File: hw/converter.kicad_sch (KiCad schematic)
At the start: 13 parts, among them J301 1935776, J302 1935776, Q301 SW_L, Q302 SW_H

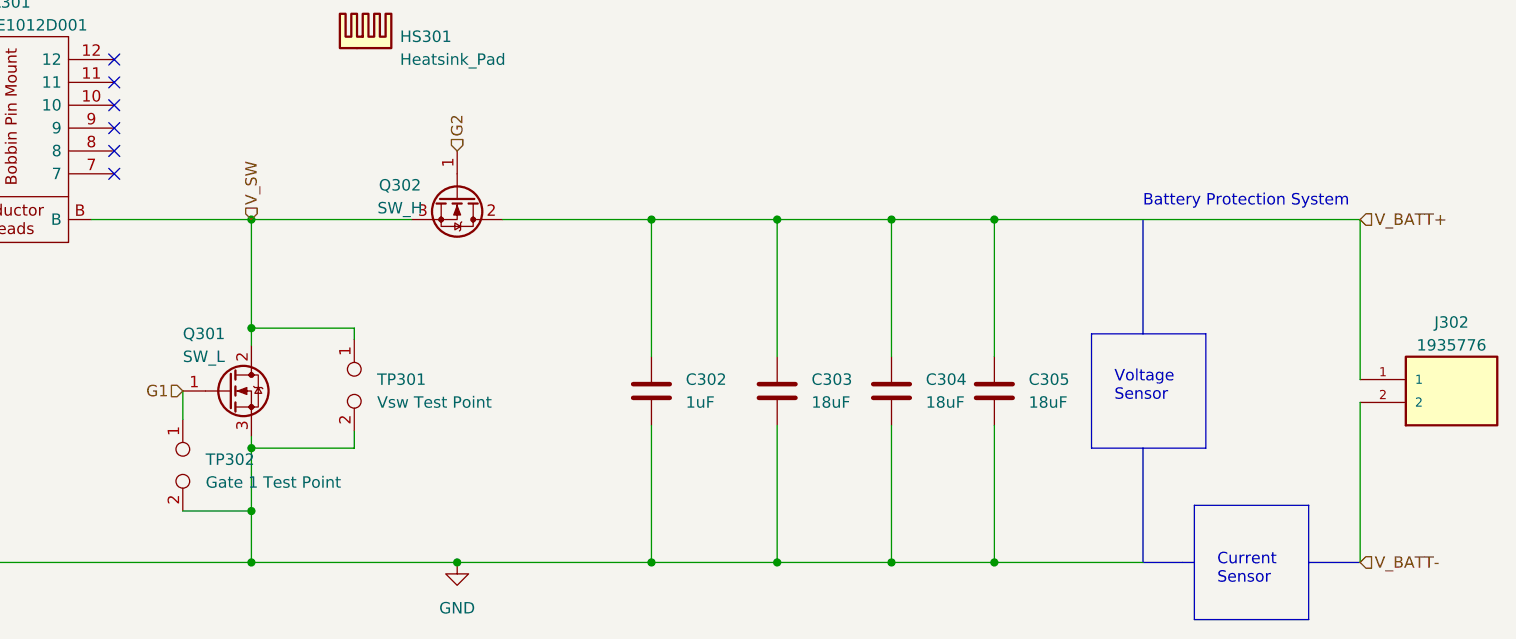
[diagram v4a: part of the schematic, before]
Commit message: rebuild schematic, passes ERC, bom completed
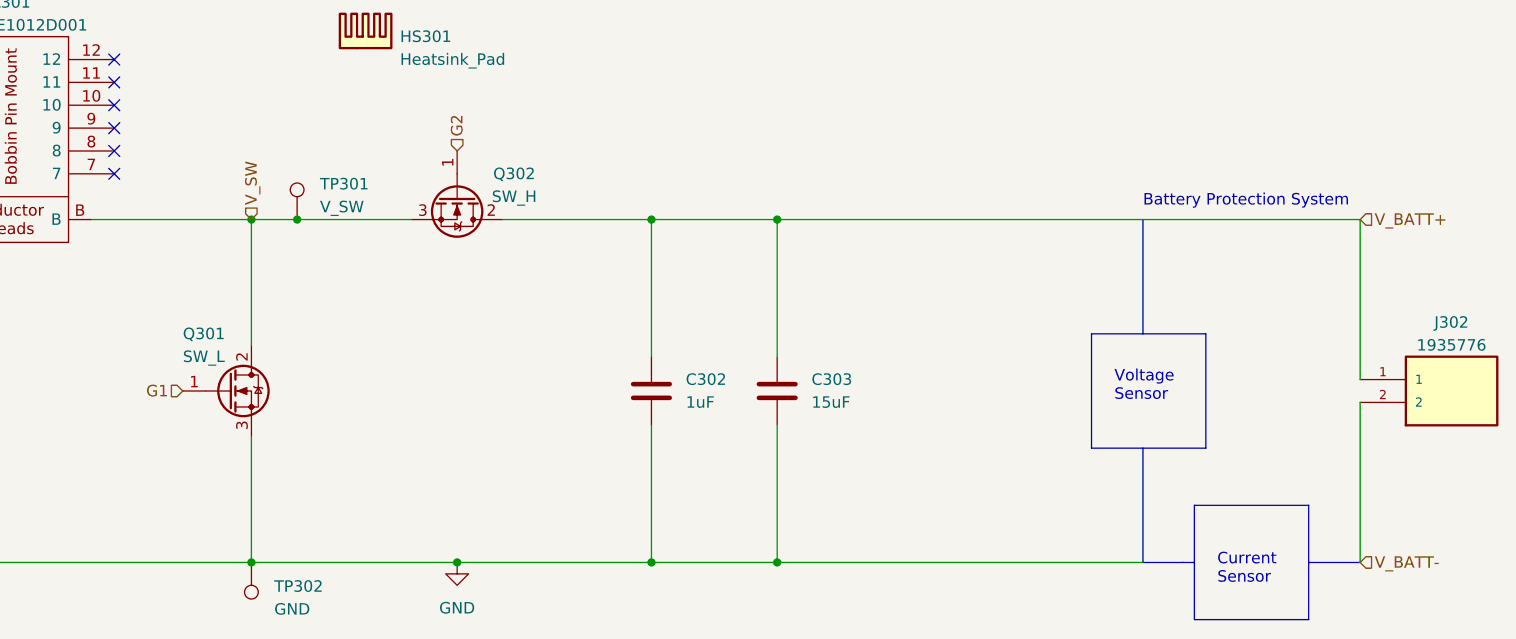
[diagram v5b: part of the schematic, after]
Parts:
- removed C304, C305: 18uF, Capacitor_THT:CP_Radial_D10.0mm_P5.00mm, symbol Device:C
- removed TP301: Vsw Test Point, mppt:SignalTP, symbol Connector:TestPoint_2Pole
- removed TP302: Gate 1 Test Point, mppt:SignalTP, symbol Connector:TestPoint_2Pole
- added TP301: V_SW, TestPoint:TestPoint_Keystone_5000-5004_Miniature, symbol Connector:TestPoint
- added TP302: GND, TestPoint:TestPoint_Keystone_5000-5004_Miniature, symbol Connector:TestPoint
- C301: footprint Capacitor_THT:CP_Axial_L10.0mm_D6.0mm_P15.00mm_Horizontal -> Capacitor_THT:C_Rect_L11.5mm_W5.6mm_P10.00mm_MKT; Distributor (none) -> Mouser; Manufacturer (none) -> Cornell Dubilier; P/N (none) -> 598-RA4505K100-FA
- C302: Distributor (none) -> Mouser; Manufacturer (none) -> TDK; P/N (none) -> 810-CGA9P3X7T2E225MA
- C303: value 18uF -> 15uF; footprint Capacitor_THT:CP_Radial_D10.0mm_P5.00mm -> Capacitor_THT:C_Rect_L41.5mm_W20.0mm_P37.50mm_MKS4; Distributor (none) -> Mouser; Manufacturer (none) -> KEMET; P/N (none) -> 80-R75GW515050H0J
- HS301: Distributor (none) -> Amazon; Manufacturer (none) -> WayInTop; P/N (none) -> N/A
- J301, J302: footprint 1935776 -> mppt:1935776; DESCRIPTION Fixed Terminal Blocks PT 2.5/ 2-5.0-H g -> (none); Distributor (none) -> Mouser; HEIGHT 13.5mm -> (none); MANUFACTURER_NAME Phoenix Contact -> (none); MANUFACTURER_PART_NUMBER 1935776 -> (none); MOUSER_PART_NUMBER 651-1935776 -> (none); MOUSER_PRICE-STOCK https://www.mouser.co.uk/ProductDetail/Phoenix-Contact/1935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 -> (none); Manufacturer (none) -> Phoenix Contact; P/N (none) -> 651-1935776
- L301: Distributor (none) -> Mouser; Height 29.3 -> (none); Manufacturer (none) -> EPCOS/TDK; Manufacturer_Name TDK -> (none); Manufacturer_Part_Number B65878E1012D001 -> (none); Mouser Part Number 871-B65878E1012D001 -> (none); Mouser Price/Stock https://www.mouser.co.uk/ProductDetail/EPCOS-TDK/B65878E101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 -> (none); P/N (none) -> 871-B65877A0000R097 / 871-B65878E1012D001
- Q301, Q302: Distributor (none) -> Digikey; Manufacturer (none) -> EPC; P/N (none) -> 917-EPC2307ENGRTTR-ND
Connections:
- net GND: now also TP302.1
- net V_SW: now also TP301.1

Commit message: savestate layout
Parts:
- removed TP301: V_SW, TestPoint:TestPoint_Keystone_5000-5004_Miniature, symbol Connector:TestPoint
- removed TP302: GND, TestPoint:TestPoint_Keystone_5000-5004_Miniature, symbol Connector:TestPoint
- added TP301: TestPoint_2Pole, mppt:SignalTP, symbol Connector:TestPoint_2Pole
- C303: value 15uF -> 18uF; footprint Capacitor_THT:C_Rect_L41.5mm_W20.0mm_P37.50mm_MKS4 -> Capacitor_THT:C_Radial_D10.0mm_H16.0mm_P5.00mm; P/N 80-R75GW515050H0J -> 80-A759MS186M2CAAE90
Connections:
- net GND: now also TP301.2
- net V_SW: now also TP301.1
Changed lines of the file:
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@@
   (junction (at 191.77 109.22) (diameter 0) (color 0 0 0 0)
   )
-  (junction (at 138.43 71.12) (diameter 0) (color 0 0 0 0)
-  )
   (junction (at 80.01 109.22) (diameter 0) (color 0 0 0 0)
   )
@@
   (junction (at 133.35 71.12) (diameter 0) (color 0 0 0 0)
   )
+  (junction (at 133.35 85.09) (diameter 0) (color 0 0 0 0)
+  )
   (junction (at 133.35 109.22) (diameter 0) (color 0 0 0 0)
   )
@@
   )
   (junction (at 156.21 109.22) (diameter 0) (color 0 0 0 0)
+  )
+  (junction (at 133.35 95.25) (diameter 0) (color 0 0 0 0)
   )
   (junction (at 177.8 109.22) (diameter 0) (color 0 0 0 0)
@@
     (stroke (width 0) (type default))
   )
+  (wire (pts (xy 133.35 85.09) (xy 140.97 85.09))
+    (stroke (width 0) (type default))
+  )
   (wire (pts (xy 40.64 91.44) (xy 40.64 109.22))
     (stroke (width 0) (type default))
@@
     (stroke (width 0) (type default))
   )
-  (wire (pts (xy 133.35 71.12) (xy 138.43 71.12))
+  (wire (pts (xy 133.35 71.12) (xy 151.13 71.12))
     (stroke (width 0) (type default))
   )
@@
     (stroke (width 0) (type default))
   )
-  (wire (pts (xy 138.43 71.12) (xy 151.13 71.12))
-    (stroke (width 0) (type default))
-  )
   (wire (pts (xy 80.01 109.22) (xy 80.01 93.98))
     (stroke (width 0) (type default))
@@
   )
   (polyline (pts (xy 60.325 115.57) (xy 47.625 115.57))
+    (stroke (width 0) (type default))
+  )
+  (wire (pts (xy 133.35 95.25) (xy 140.97 95.25))
     (stroke (width 0) (type default))
   )
@@
     )
   )
-  (symbol (lib_id "Connector:TestPoint") (at 133.35 109.22 180) (unit 1)
-    (in_bom yes) (on_board yes) (dnp no) (fields_autoplaced)
-    (property "Reference" "TP302" (at 135.89 111.887 0)
-      (effects (font (size 1.27 1.27)) (justify right))
-    )
-    (property "Value" "GND" (at 135.89 114.427 0)
-      (effects (font (size 1.27 1.27)) (justify right))
-    )
-    (property "Footprint" "TestPoint:TestPoint_Keystone_5000-5004_Miniature" (at 128.27 109.22 0)
-      (effects (font (size 1.27 1.27)) hide)
-    )
-    (property "Datasheet" "https://www.mouser.com/datasheet/2/215/000-5004-741181.pdf" (at 128.27 109.22 0)
-      (effects (font (size 1.27 1.27)) hide)
-    )
-    (property "Color" "Black" (at 133.35 109.22 0)
-      (effects (font (size 1.27 1.27)) hide)
-    )
-    (property "Distributor" "Mouser" (at 133.35 109.22 0)
-      (effects (font (size 1.27 1.27)) hide)
-    )
-    (property "Manufacturer" "Keystone Electronics" (at 133.35 109.22 0)
-      (effects (font (size 1.27 1.27)) hide)
-    )
-    (property "P/N" "534-5001" (at 133.35 109.22 0)
-      (effects (font (size 1.27 1.27)) hide)
-    )
-    (pin "1")
-    (instances
-      (project "mppt"
-        (path "/06fd3a42-664d-41bc-bf0f-b5ee0ddcc902/9cd55a57-0ec8-481d-b571-b5fdbe353ce7"
-          (reference "TP302") (unit 1)
-        )
-      )
-    )
-  )
   (symbol (lib_id "Device:C") (at 177.8 90.17 0) (unit 1)
     (in_bom yes) (on_board yes) (dnp no)
@@
     )
   )
-  (symbol (lib_id "Connector:TestPoint") (at 138.43 71.12 0) (unit 1)
-    (in_bom yes) (on_board yes) (dnp no) (fields_autoplaced)
-    (property "Reference" "TP301" (at 140.97 67.183 0)
-      (effects (font (size 1.27 1.27)) (justify left))
-    )
-    (property "Value" "V_SW" (at 140.97 69.723 0)
-      (effects (font (size 1.27 1.27)) (justify left))
-    )
-    (property "Footprint" "TestPoint:TestPoint_Keystone_5000-5004_Miniature" (at 143.51 71.12 0)
-      (effects (font (size 1.27 1.27)) hide)
-    )
-    (property "Datasheet" "https://www.mouser.com/datasheet/2/215/5115_5119-741190.pdf" (at 143.51 71.12 0)
-      (effects (font (size 1.27 1.27)) hide)
-    )
-    (property "Color" "Purple" (at 138.43 71.12 0)
-      (effects (font (size 1.27 1.27)) hide)
-    )
-    (property "Distributor" "Mouser" (at 138.43 71.12 0)
-      (effects (font (size 1.27 1.27)) hide)
-    )
-    (property "Manufacturer" "Keystone Electronics" (at 138.43 71.12 0)
-      (effects (font (size 1.27 1.27)) hide)
-    )
-    (property "P/N" "534-5119" (at 138.43 71.12 0)
-      (effects (font (size 1.27 1.27)) hide)
-    )
-    (pin "1")
-    (instances
-      (project "mppt"
-        (path "/06fd3a42-664d-41bc-bf0f-b5ee0ddcc902/9cd55a57-0ec8-481d-b571-b5fdbe353ce7"
-          (reference "TP301") (unit 1)
-        )
-      )
-    )
-  )
   (symbol (lib_id "Device:Q_NMOS_GDS") (at 156.21 68.58 270) (unit 1)
     (in_bom yes) (on_board yes) (dnp no)
@@
     )
   )
+  (symbol (lib_id "Connector:TestPoint_2Pole") (at 140.97 90.17 270) (unit 1)
+    (in_bom yes) (on_board yes) (dnp no) (fields_autoplaced)
+    (property "Reference" "TP301" (at 143.51 89.535 90)
+      (effects (font (size 1.27 1.27)) (justify left))
+    )
+    (property "Value" "TestPoint_2Pole" (at 143.51 92.075 90)
+      (effects (font (size 1.27 1.27)) (justify left))
+    )
+    (property "Footprint" "mppt:SignalTP" (at 140.97 90.17 0)
+      (effects (font (size 1.27 1.27)) hide)
+    )
+    (property "Datasheet" "~" (at 140.97 90.17 0)
+      (effects (font (size 1.27 1.27)) hide)
+    )
+    (pin "1")
+    (pin "2")
+    (instances
+      (project "mppt"
+        (path "/06fd3a42-664d-41bc-bf0f-b5ee0ddcc902/9cd55a57-0ec8-481d-b571-b5fdbe353ce7"
+          (reference "TP301") (unit 1)
+        )
+      )
+    )
+  )
   (symbol (lib_id "Device:C") (at 80.01 90.17 0) (unit 1)
     (in_bom yes) (on_board yes) (dnp no) (fields_autoplaced)
@@
       (effects (font (size 1.27 1.27)) (justify left))
     )
-    (property "Value" "15uF" (at 195.58 91.4399 0)
-      (effects (font (size 1.27 1.27)) (justify left))
-    )
-    (property "Footprint" "Capacitor_THT:C_Rect_L41.5mm_W20.0mm_P37.50mm_MKS4" (at 192.7352 93.98 0)
-      (effects (font (size 1.27 1.27)) hide)
-    )
-    (property "Datasheet" "https://www.mouser.com/datasheet/2/212/1/KEM_F3121_R75H-1879088.pdf" (at 191.77 90.17 0)
+    (property "Value" "18uF" (at 195.58 91.4399 0)
+      (effects (font (size 1.27 1.27)) (justify left))
+    )
+    (property "Footprint" "Capacitor_THT:C_Radial_D10.0mm_H16.0mm_P5.00mm" (at 192.7352 93.98 0)
+      (effects (font (size 1.27 1.27)) hide)
+    )
+    (property "Datasheet" "https://www.mouser.com/datasheet/2/212/KEM_A4072_A759-1104329.pdf" (at 191.77 90.17 0)
       (effects (font (size 1.27 1.27)) hide)
     )
@@
       (effects (font (size 1.27 1.27)) hide)
     )
-    (property "P/N" "80-R75GW515050H0J" (at 191.77 90.17 0)
-      (effects (font (size 1.27 1.27)) hide)
-    )
+    (property "P/N" "80-A759MS186M2CAAE90" (at 191.77 90.17 0)
+      (effects (font (size 1.27 1.27)) hide)
+    )

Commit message: final layout
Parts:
- added C302: CP, Capacitor_THT:C_Radial_D10.0mm_H12.5mm_P5.00mm, symbol Device:C
- added D301: Schottky, Diode_THT:D_5W_P5.08mm_Vertical_AnodeUp, symbol Device:D_Schottky
- added R301: R, Resistor_THT:R_Radial_Power_L11.0mm_W7.0mm_P5.00mm, symbol Device:R
- added TP410: TestPoint_2Pole, mppt:SignalTP, symbol Connector:TestPoint_2Pole
- renumbered C302 to C303, C303 to C304, TP301 to TP302
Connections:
- net GND: now also C302.2, TP410.2
- net V_SW: now also D301.2 (A), R301.1
- new net: C302.1, D301.1 (K), R301.2, TP410.1
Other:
- moved on the sheet: Q301, TP302

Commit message: temp for matthew to stitch
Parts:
- added C305: 18uF, Capacitor_THT:C_Radial_D10.0mm_H16.0mm_P5.00mm, symbol Device:C
- added D1: D_TVS, symbol Device:D_TVS
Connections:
- net GND: now also C305.2
- net V_BATT+: now also C305.1
- net Vsnub: now reaches C302.1, D301.1 (K), R301.2, TP410.1
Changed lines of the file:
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@@
   (junction (at 120.65 82.55) (diameter 0) (color 0 0 0 0)
   )
+  (junction (at 203.835 71.12) (diameter 0) (color 0 0 0 0)
+  )
   (junction (at 80.01 109.22) (diameter 0) (color 0 0 0 0)
   )
@@
   )
   (junction (at 146.05 109.22) (diameter 0) (color 0 0 0 0)
+  )
+  (junction (at 203.835 109.22) (diameter 0) (color 0 0 0 0)
   )
   (junction (at 146.05 85.09) (diameter 0) (color 0 0 0 0)
@@
   (no_connect (at 118.11 55.88))
   (no_connect (at 95.25 66.04))
+  (wire (pts (xy 203.835 71.12) (xy 256.54 71.12))
+    (stroke (width 0) (type default))
+  )
   (polyline (pts (xy 66.04 71.12) (xy 66.04 83.82))
     (stroke (width 0) (type default))
@@
     (stroke (width 0) (type default))
   )
+  (wire (pts (xy 203.835 93.98) (xy 203.835 109.22))
+    (stroke (width 0) (type default))
+  )
   (wire (pts (xy 191.77 93.98) (xy 191.77 109.22))
     (stroke (width 0) (type default))
@@
     (stroke (width 0) (type default))
   )
+  (wire (pts (xy 203.835 71.12) (xy 203.835 86.36))
+    (stroke (width 0) (type default))
+  )
   (wire (pts (xy 177.8 71.12) (xy 191.77 71.12))
     (stroke (width 0) (type default))
@@
     (stroke (width 0) (type default))
   )
-  (wire (pts (xy 191.77 109.22) (xy 232.41 109.22))
+  (wire (pts (xy 191.77 109.22) (xy 203.835 109.22))
     (stroke (width 0) (type default))
   )
@@
     (stroke (width 0) (type default))
   )
+  (wire (pts (xy 203.835 109.22) (xy 232.41 109.22))
+    (stroke (width 0) (type default))
+  )
   (wire (pts (xy 115.57 102.87) (xy 120.65 102.87))
     (stroke (width 0) (type default))
@@
     (stroke (width 0) (type default))
   )
-  (wire (pts (xy 191.77 71.12) (xy 256.54 71.12))
+  (wire (pts (xy 191.77 71.12) (xy 203.835 71.12))
     (stroke (width 0) (type default))
   )
@@
   )
   (text "Current\nSensor" (at 50.165 111.76 0)
+    (effects (font (size 1.27 1.27)) (justify left bottom))
+  )
+  (label "Vsnub" (at 125.73 92.71 0) (fields_autoplaced)
     (effects (font (size 1.27 1.27)) (justify left bottom))
   )
@@
     )
   )
+  (symbol (lib_id "Device:D_TVS") (at 168.275 85.09 90) (unit 1)
+    (in_bom yes) (on_board yes) (dnp no) (fields_autoplaced)
+    (property "Reference" "D1" (at 171.45 84.455 90)
+      (effects (font (size 1.27 1.27)) (justify right))
+    )
+    (property "Value" "D_TVS" (at 171.45 86.995 90)
+      (effects (font (size 1.27 1.27)) (justify right))
+    )
+    (property "Footprint" "" (at 168.275 85.09 0)
+      (effects (font (size 1.27 1.27)) hide)
+    )
+    (property "Datasheet" "~" (at 168.275 85.09 0)
+      (effects (font (size 1.27 1.27)) hide)
+    )
+    (pin "1")
+    (pin "2")
+    (instances
+      (project "mppt"
+        (path "/06fd3a42-664d-41bc-bf0f-b5ee0ddcc902/9cd55a57-0ec8-481d-b571-b5fdbe353ce7"
+          (reference "D1") (unit 1)
+        )
+      )
+    )
+  )
   (symbol (lib_id "Device:D_Schottky") (at 125.73 86.36 90) (unit 1)
     (in_bom yes) (on_board yes) (dnp no)
@@
         )
       )
+    )
+  )
+  (symbol (lib_id "Device:C") (at 203.835 90.17 0) (unit 1)
+    (in_bom yes) (on_board yes) (dnp no)
+    (property "Reference" "C305" (at 207.645 88.8999 0)
+      (effects (font (size 1.27 1.27)) (justify left))
+    )
+    (property "Value" "18uF" (at 207.645 91.4399 0)
+      (effects (font (size 1.27 1.27)) (justify left))
+    )
+    (property "Footprint" "Capacitor_THT:C_Radial_D10.0mm_H16.0mm_P5.00mm" (at 204.8002 93.98 0)
+      (effects (font (size 1.27 1.27)) hide)
+    )
+    (property "Datasheet" "https://www.mouser.com/datasheet/2/212/KEM_A4072_A759-1104329.pdf" (at 203.835 90.17 0)
+      (effects (font (size 1.27 1.27)) hide)
+    )
+    (property "Distributor" "Mouser" (at 203.835 90.17 0)
+      (effects (font (size 1.27 1.27)) hide)
+    )
+    (property "JLC P/N" "" (at 203.835 90.17 0)
+      (effects (font (size 1.27 1.27)) hide)
+    )
+    (property "Manufacturer" "KEMET" (at 203.835 90.17 0)
+      (effects (font (size 1.27 1.27)) hide)
+    )
+    (property "P/N" "80-A759MS186M2CAAE90" (at 203.835 90.17 0)
+      (effects (font (size 1.27 1.27)) hide)
+    )
+    (pin "1")
+    (pin "2")
+    (instances
+      (project "mppt"
+        (path "/06fd3a42-664d-41bc-bf0f-b5ee0ddcc902/9cd55a57-0ec8-481d-b571-b5fdbe353ce7"
+          (reference "C305") (unit 1)
+        )
+      )
